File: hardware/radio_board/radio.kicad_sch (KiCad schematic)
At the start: 29 parts, among them J2 Conn_Coaxial, J3 RFShield_OnePiece

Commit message: Update to 4 radio board in progress
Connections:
- net +3.3V renamed 3v3_local
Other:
- moved on the sheet: C1, C10, C11, C12, C13, C14, C15, C2, C3, C4, C5, C9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

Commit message: Wire up 4 radios
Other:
- moved on the sheet: C13, C14, C4, C5, R1

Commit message: Layout in progress
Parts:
- J2: value Conn_Coaxial -> RF
- J3: value RFShield_OnePiece -> Shield
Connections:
- net GNDA renamed AGND_local
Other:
- moved on the sheet: C6, C7, C8, FB1, R2

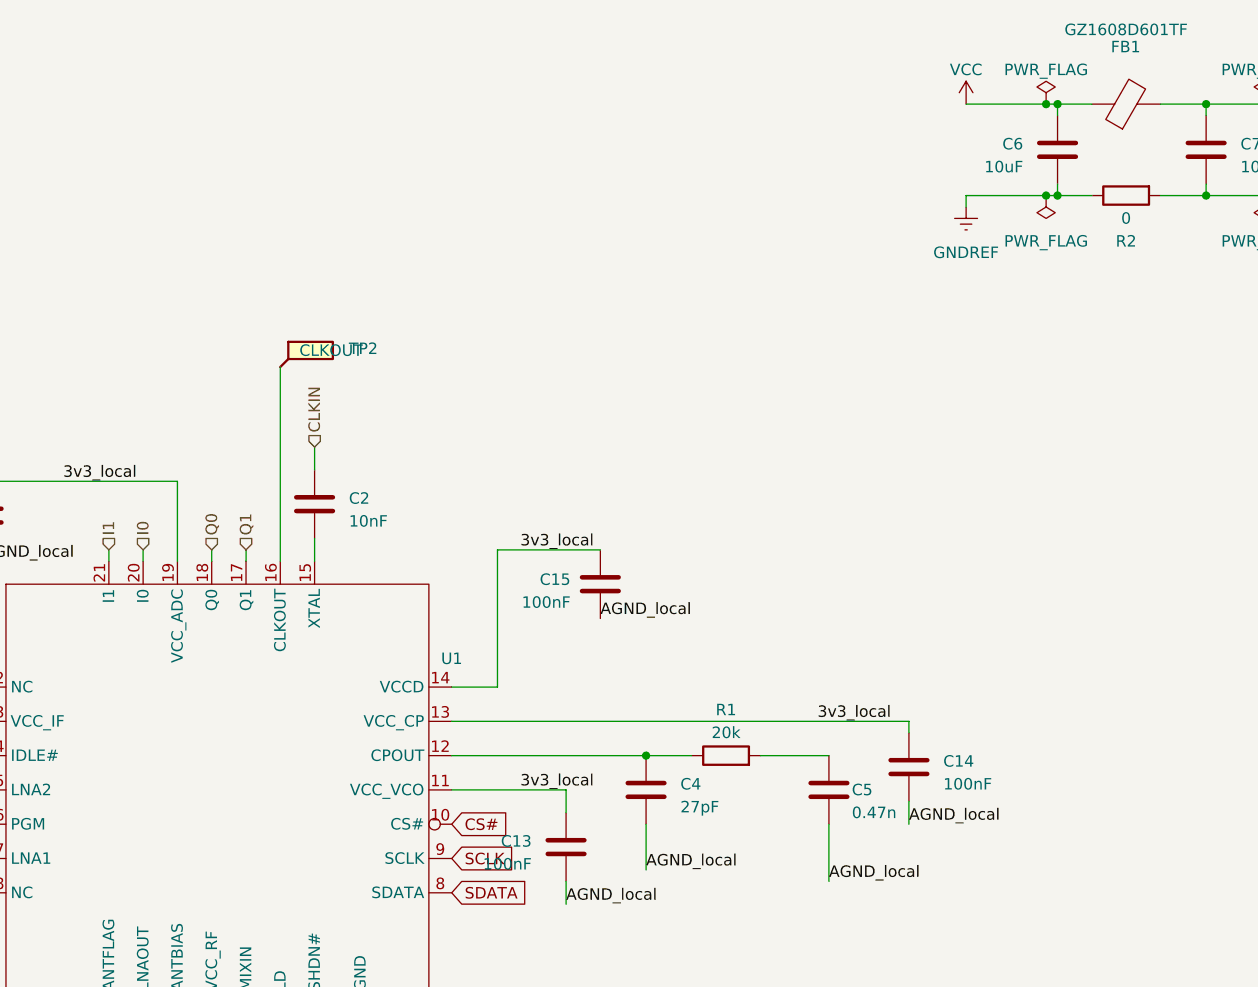
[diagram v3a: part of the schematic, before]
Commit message: First radio layout done
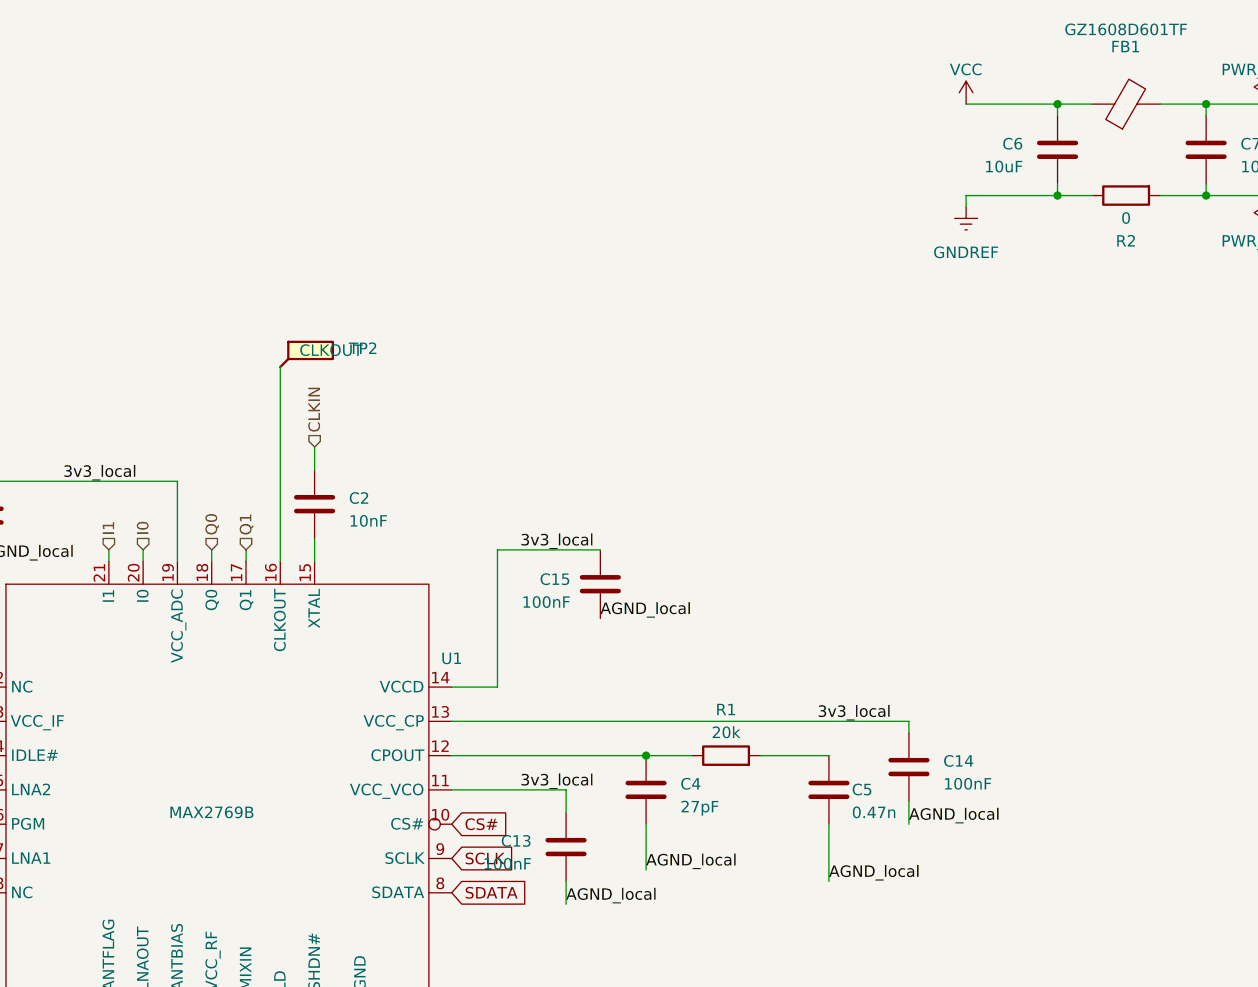
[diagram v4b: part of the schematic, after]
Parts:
- U1: value ~ -> MAX2769B
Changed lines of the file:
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@@
   (junction (at 229.87 38.1) (diameter 0) (color 0 0 0 0)
-  )
-  (junction (at 228.6 27.94) (diameter 0) (color 0 0 0 0)
-  )
-  (junction (at 228.6 38.1) (diameter 0) (color 0 0 0 0)
   )
   (junction (at 259.08 38.1) (diameter 0) (color 0 0 0 0)
@@
     (stroke (width 0) (type default))
   )
-  (wire (pts (xy 228.6 27.94) (xy 229.87 27.94))
-    (stroke (width 0) (type default))
-  )
   (wire (pts (xy 175.26 104.14) (xy 175.26 106.68))
     (stroke (width 0) (type default))
@@
     (stroke (width 0) (type default))
   )
-  (wire (pts (xy 228.6 38.1) (xy 229.87 38.1))
+  (wire (pts (xy 219.71 38.1) (xy 229.87 38.1))
     (stroke (width 0) (type default))
   )
@@
     (stroke (width 0) (type default))
   )
-  (wire (pts (xy 219.71 38.1) (xy 228.6 38.1))
-    (stroke (width 0) (type default))
-  )
   (wire (pts (xy 259.08 38.1) (xy 265.43 38.1))
     (stroke (width 0) (type default))
@@
     (stroke (width 0) (type default))
   )
-  (wire (pts (xy 219.71 27.94) (xy 228.6 27.94))
+  (wire (pts (xy 219.71 27.94) (xy 229.87 27.94))
     (stroke (width 0) (type default))
   )
@@
     )
   )
-  (symbol (lib_id "power:PWR_FLAG") (at 228.6 27.94 0) (unit 1)
-    (in_bom yes) (on_board yes) (dnp no) (fields_autoplaced)
-    (property "Reference" "#FLG03" (at 228.6 26.035 0)
-      (effects (font (size 1.27 1.27)) hide)
-    )
-    (property "Value" "PWR_FLAG" (at 228.6 24.13 0)
-      (effects (font (size 1.27 1.27)))
-    )
-    (property "Footprint" "" (at 228.6 27.94 0)
-      (effects (font (size 1.27 1.27)) hide)
-    )
-    (property "Datasheet" "~" (at 228.6 27.94 0)
-      (effects (font (size 1.27 1.27)) hide)
-    )
-    (pin "1")
-    (instances
-      (project "design"
-        (path "/6dbd6c42-edf6-461d-b7ca-066e49b0019c"
-          (reference "#FLG03") (unit 1)
-        )
-        (path "/6dbd6c42-edf6-461d-b7ca-066e49b0019c/78691f3e-c8cc-4de2-b4f7-4d5d660bca23"
-          (reference "#FLG01") (unit 1)
-        )
-        (path "/6dbd6c42-edf6-461d-b7ca-066e49b0019c/1b895c4a-56fd-4590-a8aa-7507dccb37cf"
-          (reference "#FLG05") (unit 1)
-        )
-        (path "/6dbd6c42-edf6-461d-b7ca-066e49b0019c/bbad701b-ab9c-48bf-af04-0d262cb749b1"
-          (reference "#FLG09") (unit 1)
-        )
-        (path "/6dbd6c42-edf6-461d-b7ca-066e49b0019c/f20fbf31-47b8-4912-9caa-c1ed256d71c4"
-          (reference "#FLG013") (unit 1)
-        )
-      )
-    )
-  )
   (symbol (lib_id "Device:R") (at 38.1 109.22 0) (unit 1)
     (in_bom yes) (on_board yes) (dnp no) (fields_autoplaced)
@@
   )
   (symbol (lib_id "tart:Max2769BETI") (at 135.89 104.14 0) (unit 1)
-    (in_bom yes) (on_board yes) (dnp no) (fields_autoplaced)
+    (in_bom yes) (on_board yes) (dnp no)
     (property "Reference" "U1" (at 162.56 89.5603 0)
       (effects (font (size 1.27 1.27)))
     )
-    (property "Value" "~" (at 162.56 143.51 0)
+    (property "Value" "MAX2769B" (at 135.89 106.68 0)
       (effects (font (size 1.27 1.27)))
     )
@@
       (effects (font (size 1.27 1.27)) hide)
     )
-    (pin "1")
     (pin "11")
     (pin "12")
@@
     (pin "17")
     (pin "18")
-    (pin "2")
     (pin "20")
     (pin "21")
@@
     (pin "27")
     (pin "28")
+    (pin "9")
+    (pin "1")
+    (pin "10")
+    (pin "19")
+    (pin "2")
     (pin "3")
     (pin "4")
@@
     (pin "7")
     (pin "8")
-    (pin "9")
-    (pin "10")
-    (pin "19")
     (pin "29")
     (instances
@@
         )
       )
-    )
-  )
-  (symbol (lib_id "power:PWR_FLAG") (at 228.6 38.1 180) (unit 1)
-    (in_bom yes) (on_board yes) (dnp no) (fields_autoplaced)
-    (property "Reference" "#FLG04" (at 228.6 40.005 0)
-      (effects (font (size 1.27 1.27)) hide)
-    )
-    (property "Value" "PWR_FLAG" (at 228.6 43.18 0)
-      (effects (font (size 1.27 1.27)))
-    )
-    (property "Footprint" "" (at 228.6 38.1 0)
-      (effects (font (size 1.27 1.27)) hide)
-    )
-    (property "Datasheet" "~" (at 228.6 38.1 0)
-      (effects (font (size 1.27 1.27)) hide)
-    )
-    (pin "1")
-    (instances
-      (project "design"
-        (path "/6dbd6c42-edf6-461d-b7ca-066e49b0019c"
-          (reference "#FLG04") (unit 1)
-        )
-        (path "/6dbd6c42-edf6-461d-b7ca-066e49b0019c/78691f3e-c8cc-4de2-b4f7-4d5d660bca23"
-          (reference "#FLG02") (unit 1)
-        )
-        (path "/6dbd6c42-edf6-461d-b7ca-066e49b0019c/1b895c4a-56fd-4590-a8aa-7507dccb37cf"
-          (reference "#FLG06") (unit 1)
-        )
-        (path "/6dbd6c42-edf6-461d-b7ca-066e49b0019c/bbad701b-ab9c-48bf-af04-0d262cb749b1"
-          (reference "#FLG010") (unit 1)
-        )
-        (path "/6dbd6c42-edf6-461d-b7ca-066e49b0019c/f20fbf31-47b8-4912-9caa-c1ed256d71c4"
-          (reference "#FLG014") (unit 1)
-        )
-      )

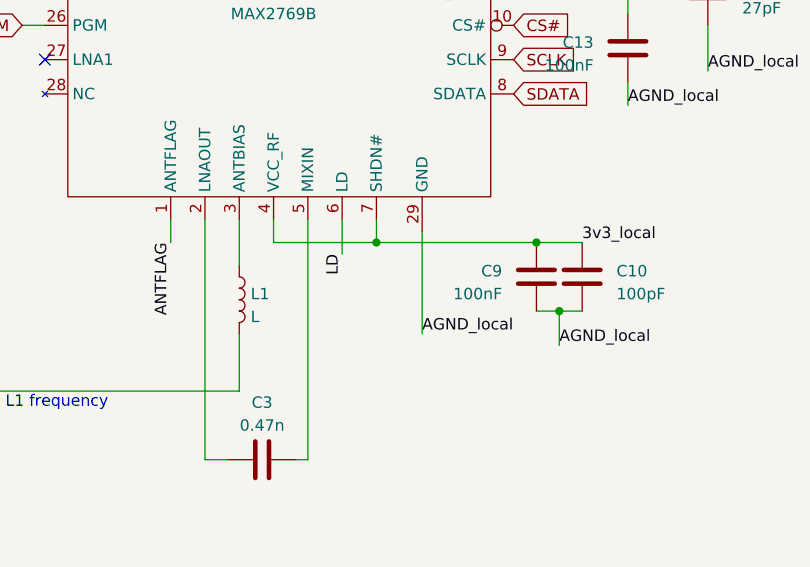
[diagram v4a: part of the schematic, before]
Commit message: Add the shutdown line to the radio board. Fix up the DIMM footprint
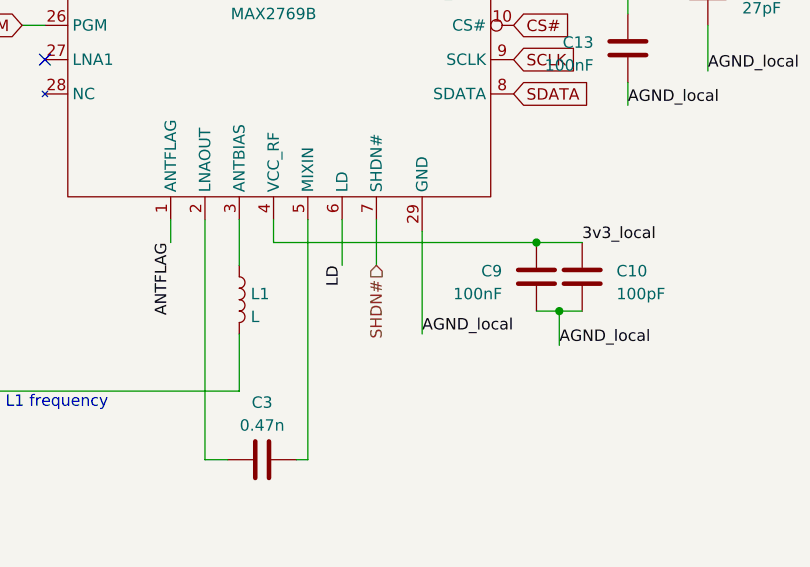
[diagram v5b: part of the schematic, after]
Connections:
- net 3v3_local: no longer U1.7 (SHDN#)
- new net SHDN#: U1.7 (SHDN#)
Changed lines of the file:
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@@
   (junction (at 184.15 100.33) (diameter 0) (color 0 0 0 0)
-  )
-  (junction (at 147.32 132.08) (diameter 0) (color 0 0 0 0)
   )
   (junction (at 165.1 132.08) (diameter 0) (color 0 0 0 0)
@@
     (stroke (width 0) (type default))
   )
+  (wire (pts (xy 147.32 129.54) (xy 147.32 134.62))
+    (stroke (width 0) (type default))
+  )
   (wire (pts (xy 246.38 38.1) (xy 246.38 36.83))
     (stroke (width 0) (type default))
@@
     (stroke (width 0) (type default))
   )
-  (wire (pts (xy 135.89 132.08) (xy 147.32 132.08))
+  (wire (pts (xy 135.89 132.08) (xy 165.1 132.08))
     (stroke (width 0) (type default))
   )
@@
     (stroke (width 0) (type default))
   )
-  (wire (pts (xy 147.32 132.08) (xy 165.1 132.08))
-    (stroke (width 0) (type default))
-  )
   (wire (pts (xy 175.26 104.14) (xy 175.26 106.68))
     (stroke (width 0) (type default))
@@
     (stroke (width 0) (type default))
   )
-  (wire (pts (xy 143.51 129.54) (xy 143.51 133.35))
+  (wire (pts (xy 143.51 129.54) (xy 143.51 134.62))
     (stroke (width 0) (type default))
   )
@@
   )
   (wire (pts (xy 229.87 38.1) (xy 233.68 38.1))
-    (stroke (width 0) (type default))
-  )
-  (wire (pts (xy 147.32 129.54) (xy 147.32 132.08))
     (stroke (width 0) (type default))
   )
@@
     (effects (font (size 1.27 1.27)) (justify left bottom))
   )
-  (label "LD" (at 143.51 133.35 270) (fields_autoplaced)
+  (label "LD" (at 143.51 134.62 270) (fields_autoplaced)
     (effects (font (size 1.27 1.27)) (justify right bottom))
   )
@@
     (effects (font (size 1.27 1.27)) (justify left))
   )
+  (hierarchical_label "SHDN#" (shape input) (at 147.32 134.62 270) (fields_autoplaced)
+    (effects (font (size 1.27 1.27)) (justify right))
+  )
   (hierarchical_label "CLKIN" (shape input) (at 147.32 66.04 90) (fields_autoplaced)

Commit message: Fix capacitor sizes
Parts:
- C8: footprint Capacitor_SMD:C_0603_1608Metric -> Capacitor_SMD:C_0402_1005Metric
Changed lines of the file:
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@@
       (effects (font (size 1.27 1.27)) (justify left))
     )
-    (property "Footprint" "Capacitor_SMD:C_0603_1608Metric" (at 260.0452 36.83 0)
+    (property "Footprint" "Capacitor_SMD:C_0402_1005Metric" (at 260.0452 36.83 0)
       (effects (font (size 1.27 1.27)) hide)
     )

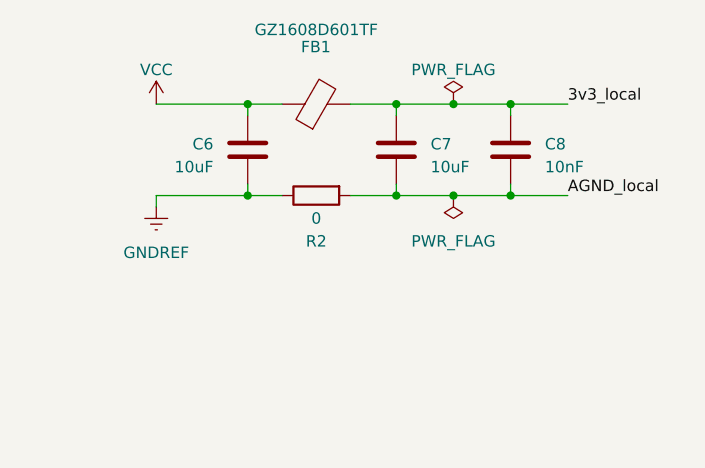
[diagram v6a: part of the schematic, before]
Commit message: Update to use edge mountyed SMA
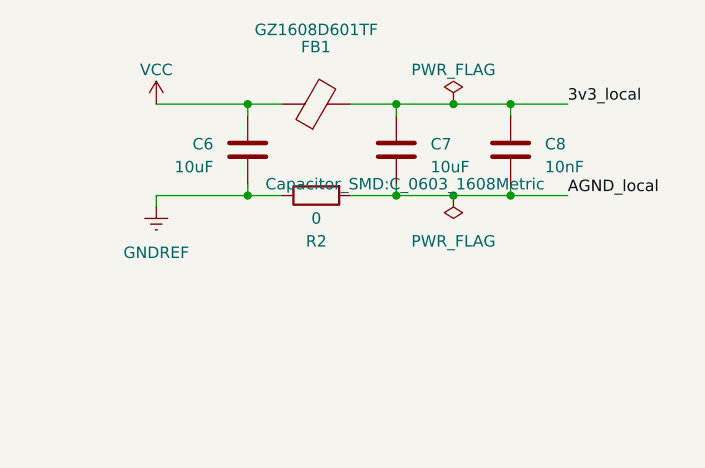
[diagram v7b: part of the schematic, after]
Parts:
- J2: footprint Connector_Coaxial:SMA_Amphenol_132291_Vertical -> radio_module:CONN-SMD_KH-SMA-KE8-G; LCSC (none) -> C530661
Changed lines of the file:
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@@
       (effects (font (size 1.27 1.27)))
     )
-    (property "Footprint" "Connector_Coaxial:SMA_Amphenol_132291_Vertical" (at 81.28 104.14 0)
+    (property "Footprint" "radio_module:CONN-SMD_KH-SMA-KE8-G" (at 81.28 104.14 0)
       (effects (font (size 1.27 1.27)) hide)
     )
     (property "Datasheet" " ~" (at 81.28 104.14 0)
+      (effects (font (size 1.27 1.27)) hide)
+    )
+    (property "LCSC" "C530661" (at 81.28 104.14 0)
       (effects (font (size 1.27 1.27)) hide)
     )
@@
     )
     (property "Footprint" "Capacitor_SMD:C_0603_1608Metric" (at 247.3452 36.83 0)
-      (effects (font (size 1.27 1.27)) hide)
+      (effects (font (size 1.27 1.27)))
     )
     (property "Datasheet" "~" (at 246.38 33.02 0)
